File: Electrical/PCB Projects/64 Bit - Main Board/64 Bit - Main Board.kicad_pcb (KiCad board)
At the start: 4 copper layers, 200 x 100 mm, 213 parts, among them J1 61301021821, J10 M20-7920242R, J11 M20-7920242R, J12 M20-7920242R, J13 M20-7920242R, J14 1985195, J2 61301021821, J3 61301021821, J4 M20-7920242R, J5 USBC, J6 M20-7920242R, J7 PJ-102A, J8 M20-7920242R, J9 M20-7920242R, K1 JS-12N-K, K2 JS-12N-K, K3 JS-12N-K, K4 PR30-5V-450-1A-E, K5 PR30-12V-450-1A-E, P1 Conn_01x02, Q1 2N7002, Q10 XP231P0201TR-G, Q11 2N7002, Q2 XP231P0201TR-G, Q3 2N7002, Q4 2N7002, Q5 2N7002, Q6 XP231P0201TR-G, Q7 XP231P0201TR-G, Q8 2N7002, Q9 2N7002, SW1 1985195, SW2 1985195, SW3 1985195, SW4 1985195, SW5 L102011MS02Q, SW6 power_switch, U1 STM32F446RETx, U2 PCA9306, U3 DS1307+, U4 74HC3G34DC, U5 74HC3G34DC, U6 74HC3G34DC, U7 EN12-VS20AF20, U8 24LC64, Y1 Crystal_GND24, Y2 32.768kHz-12.6pF, Y3 32.768kHz-12.6pF

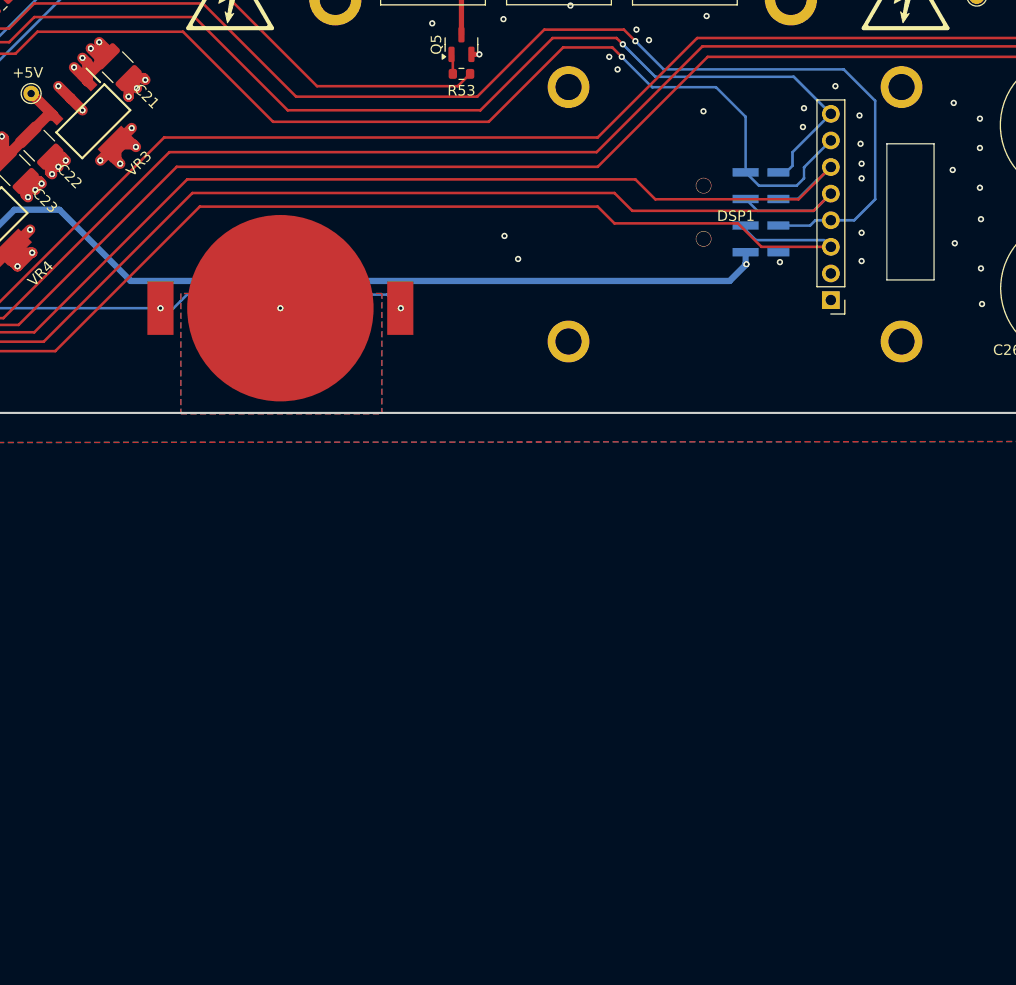
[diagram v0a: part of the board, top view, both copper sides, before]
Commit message: finalized schematic, made ESP32 footprint, started PCB update
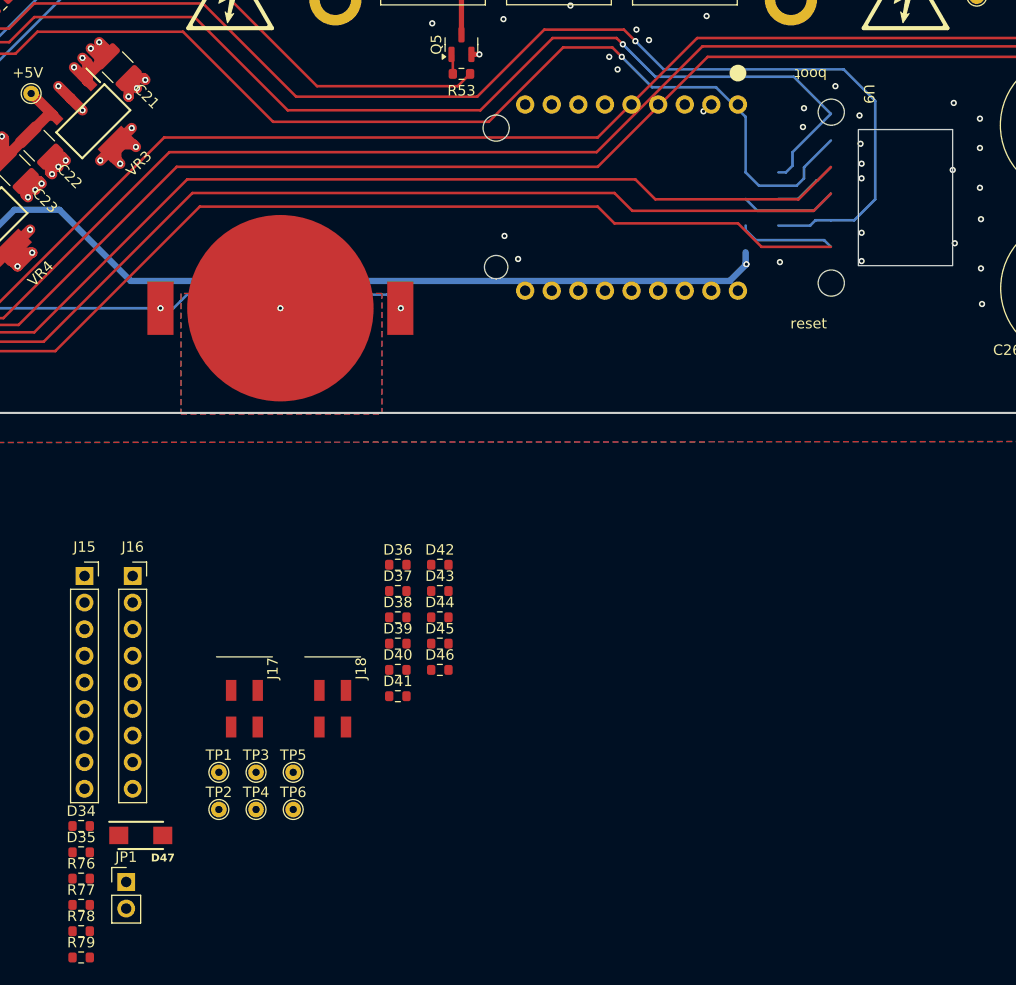
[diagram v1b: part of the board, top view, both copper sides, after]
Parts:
- removed DSP1: 610108249221, Footprint drive Dump 1:240x280 LCD
- added D34: TVS_0603, Resistor_SMD:R_0603_1608Metric, F.Cu at (133.0, 179.9)
- added D35: TVS_0603, Resistor_SMD:R_0603_1608Metric, F.Cu at (133.0, 182.5)
- added D36: TVS_0603, Resistor_SMD:R_0603_1608Metric, F.Cu at (163.2, 155.0)
- added D37: TVS_0603, Resistor_SMD:R_0603_1608Metric, F.Cu at (163.2, 157.5)
- added D38: TVS_0603, Resistor_SMD:R_0603_1608Metric, F.Cu at (163.2, 160.0)
- added D39: TVS_0603, Resistor_SMD:R_0603_1608Metric, F.Cu at (163.2, 162.5)
- added D40: TVS_0603, Resistor_SMD:R_0603_1608Metric, F.Cu at (163.2, 165.0)
- added D41: TVS_0603, Resistor_SMD:R_0603_1608Metric, F.Cu at (163.2, 167.6)
- added D42: TVS_0603, Resistor_SMD:R_0603_1608Metric, F.Cu at (167.2, 155.0)
- added D43: TVS_0603, Resistor_SMD:R_0603_1608Metric, F.Cu at (167.2, 157.5)
- added D44: TVS_0603, Resistor_SMD:R_0603_1608Metric, F.Cu at (167.2, 160.0)
- added D45: TVS_0603, Resistor_SMD:R_0603_1608Metric, F.Cu at (167.2, 162.5)
- added D46: TVS_0603, Resistor_SMD:R_0603_1608Metric, F.Cu at (167.2, 165.0)
- added D47: SK54BLF-R1_00001, Footprint drive Dump 1:SK54BLF-R1_00001, F.Cu at (138.7, 180.8)
- added J15: Conn_01x09, Connector_PinSocket_2.54mm:PinSocket_1x09_P2.54mm_Vertical, F.Cu at (133.3, 156.1)
- added J16: Conn_01x09, Connector_PinSocket_2.54mm:PinSocket_1x09_P2.54mm_Vertical, F.Cu at (137.9, 156.1)
- added J17: M20-7920242R, Footprint drive Dump 1:M207920242R, F.Cu at (148.6, 162.9)
- added J18: M20-7920242R, Footprint drive Dump 1:M207920242R, F.Cu at (157.0, 162.9)
- added JP1: Jumper_2_Open, Connector_PinHeader_2.54mm:PinHeader_1x02_P2.54mm_Vertical, F.Cu at (137.3, 185.3)
- added R76: 0ohm_0603, Resistor_SMD:R_0603_1608Metric, F.Cu at (133.0, 185.0)
- added R77: 0ohm_0603_NA, Resistor_SMD:R_0603_1608Metric, F.Cu at (133.0, 187.5)
- added R78: 0ohm_0603, Resistor_SMD:R_0603_1608Metric, F.Cu at (133.0, 190.0)
- added R79: 0ohm_0603_NA, Resistor_SMD:R_0603_1608Metric, F.Cu at (133.0, 192.5)
- added TP1: TestPoint, TestPoint:TestPoint_THTPad_D1.5mm_Drill0.7mm, F.Cu at (146.1, 174.8)
- added TP2: TestPoint, TestPoint:TestPoint_THTPad_D1.5mm_Drill0.7mm, F.Cu at (146.1, 178.4)
- added TP3: TestPoint, TestPoint:TestPoint_THTPad_D1.5mm_Drill0.7mm, F.Cu at (149.7, 174.8)
- added TP4: TestPoint, TestPoint:TestPoint_THTPad_D1.5mm_Drill0.7mm, F.Cu at (149.7, 178.4)
- added TP5: TestPoint, TestPoint:TestPoint_THTPad_D1.5mm_Drill0.7mm, F.Cu at (153.2, 174.8)
- added TP6: TestPoint, TestPoint:TestPoint_THTPad_D1.5mm_Drill0.7mm, F.Cu at (153.2, 178.4)
- added U9: ESP32-C6-LCD-1.47, Footprint drive Dump 1:ESP32-C6-LCD-1.47, F.Cu at (195.7, 111.0)
- R2, R3, R4: value 10kohm_0603 -> 1kohm_0603
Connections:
- U1 pad 10: LCD1_CS -> IO7
- U1 pad 11: LCD1_DC -> IO8
- U1 pad 24: LCD1_RST -> IO9
- U1 pad 25: LCD1_BL -> USART3_RX
- U1 pad 29: LCD_SCK -> USART3_TX
- U1 pad 9: LCD_MOSI -> IO6
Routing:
- net USART3_TX: track 0.00 -> 164.4 mm, vias 0 -> 1
- net LCD_SCK: track 164.4 -> 0.00 mm, vias 1 -> 0
- net LCD_MOSI: track 160.1 -> 0.00 mm
- net LCD1_CS: track 158.4 -> 0.00 mm
- net LCD1_DC: track 154.6 -> 0.00 mm
- net LCD1_RST: track 152.6 -> 0.00 mm, vias 1 -> 0
- net IO9: track 0.00 -> 152.6 mm, vias 0 -> 1
- net USART3_RX: track 0.00 -> 152.6 mm, vias 0 -> 1
- net LCD1_BL: track 152.6 -> 0.00 mm, vias 1 -> 0
- net IO6: track 0.00 -> 150.9 mm
- net IO7: track 0.00 -> 149.1 mm
- net IO8: track 0.00 -> 148.3 mm
- net (no net): track 0.00 -> 24.8 mm

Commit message: save for night
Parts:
- J15, J16, J17, J18: moved to B.Cu
- moved J15 76.0 mm to (196.9, 114.4), turned to 90 degrees
- moved J16 49.4 mm to (176.9, 125.7), turned to -90 degrees
- moved J18 43.2 mm to (133.7, 126.5), turned to 180 degrees
- moved J17 43.2 mm to (125.2, 126.5), turned to 180 degrees
- moved D47 42.5 mm to (174.3, 157.7)
- moved D35 34.9 mm to (158.6, 158.7)
- moved R76 34.9 mm to (158.6, 161.2)
- moved R78 34.9 mm to (158.6, 166.2)
- moved R79 34.9 mm to (158.6, 168.7)
- moved D34 34.9 mm to (158.6, 156.2)
- moved R77 34.9 mm to (158.6, 163.7)
- moved JP1 28.9 mm to (147.8, 158.4)
- moved TP2 19.3 mm to (133.1, 164.1)
- moved TP4 19.3 mm to (136.7, 164.1)
- moved TP6 19.3 mm to (140.2, 164.1)
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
